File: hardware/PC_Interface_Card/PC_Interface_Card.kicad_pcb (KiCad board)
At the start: 2 copper layers, 85 parts, among them J1 GSB1C41110SSHR, J2 DM3BT-DSF-PEJS, J3 BM11B-GHS-TBT, SW1 CherryMX, SW2 CherryMX, SW3 CherryMX, SW4 CherryMX, SW5 CherryMX, SW6 TL1240YQ2JBLK, SW7 TL1240YQ2JBLK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

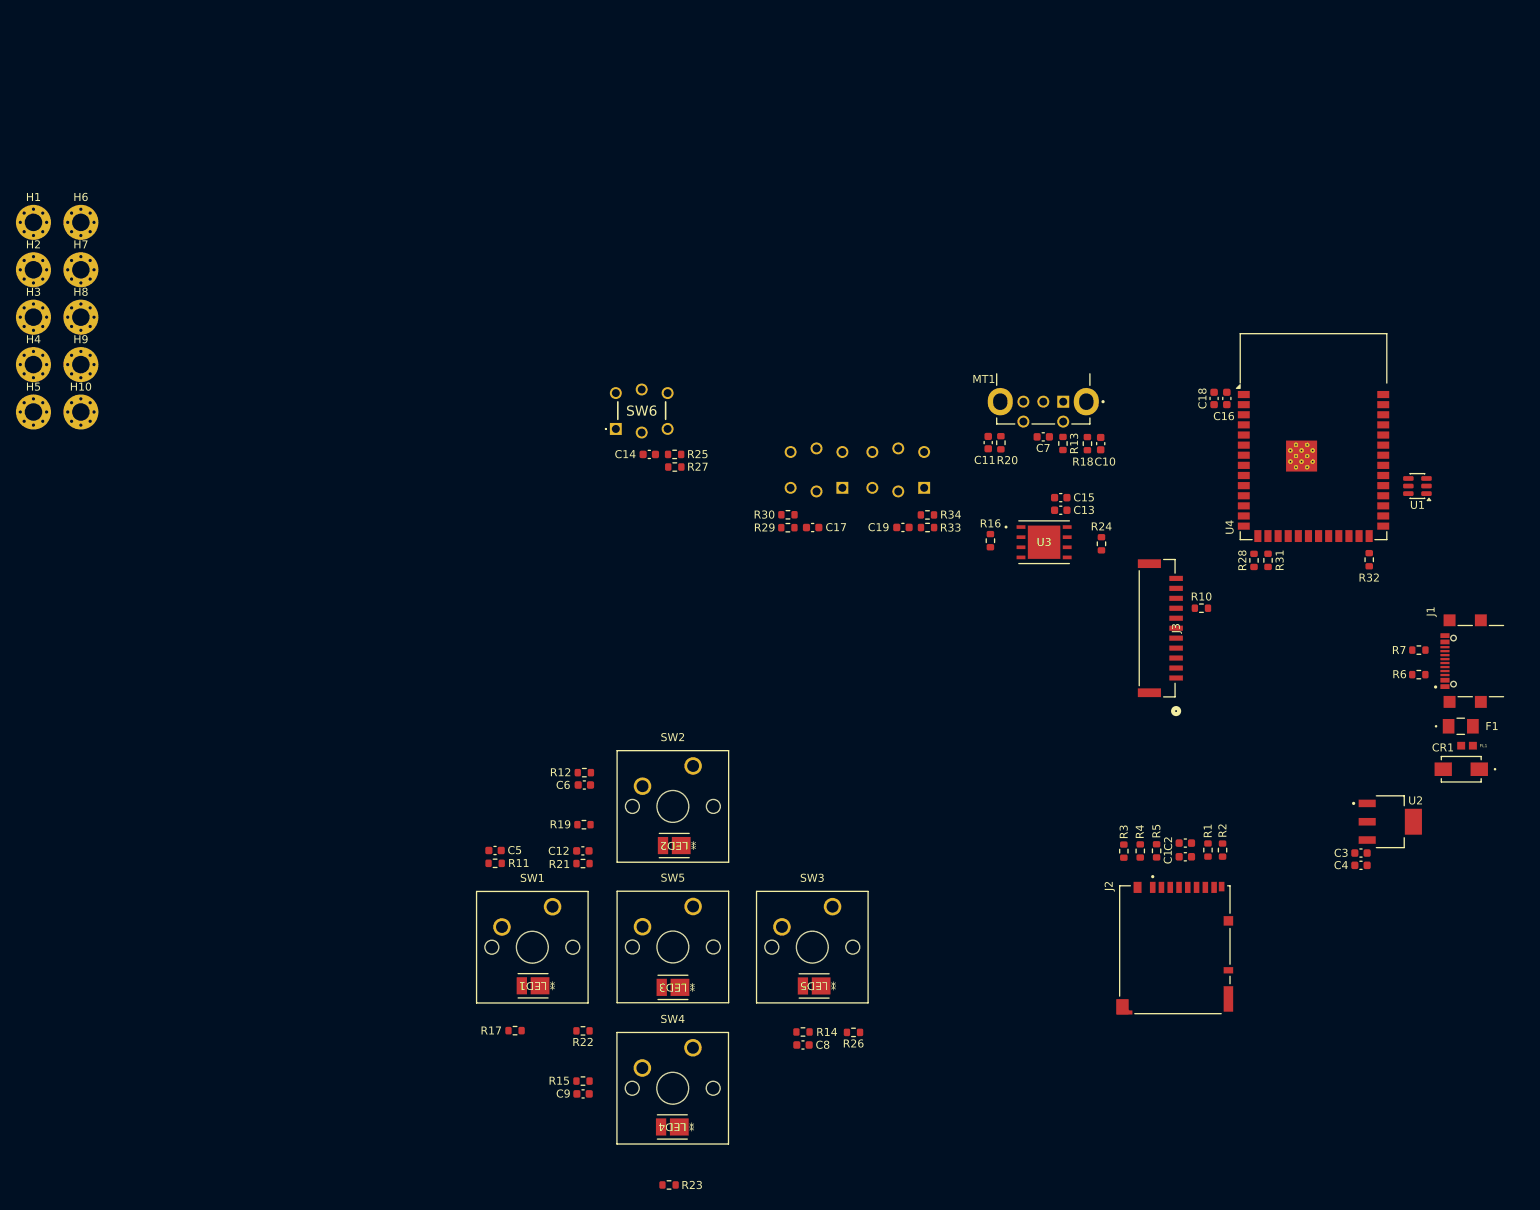
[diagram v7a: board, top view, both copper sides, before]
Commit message: Saving data for the day - added dxf for display and component placement
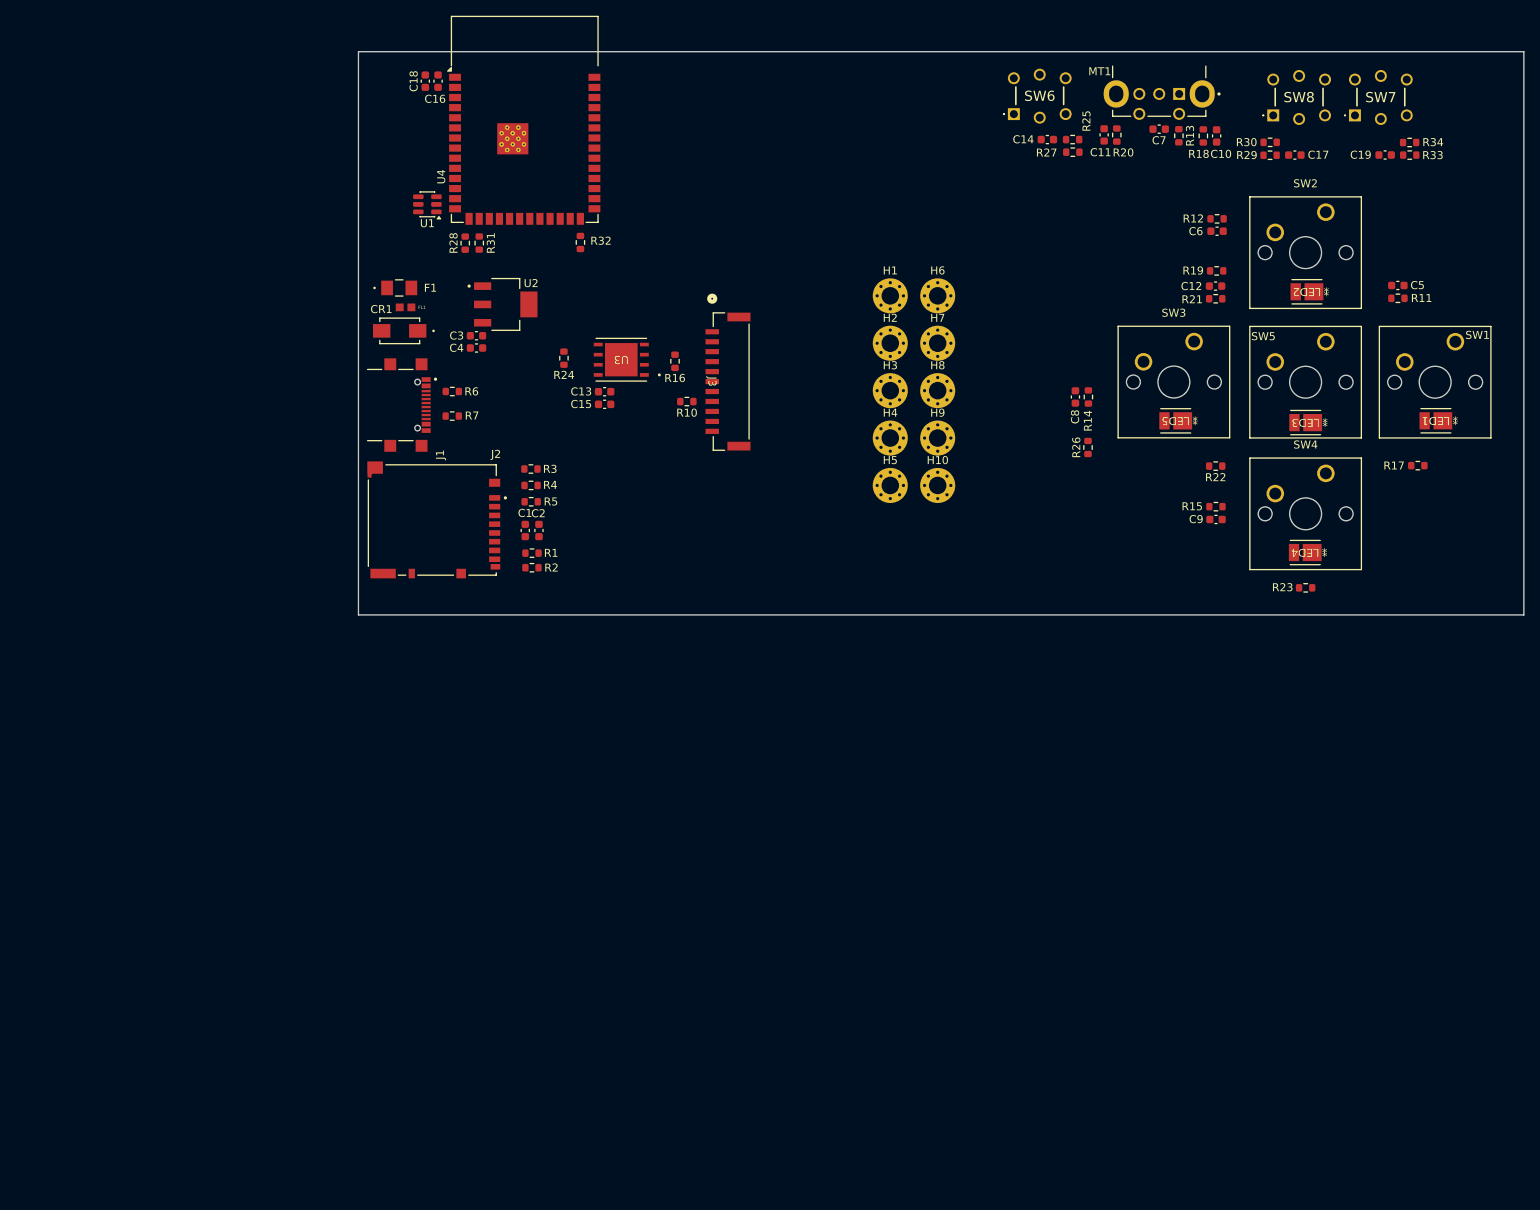
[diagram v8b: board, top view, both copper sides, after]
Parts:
- SW7, SW8: moved to F.Cu
- moved CR1 144.1 mm to (14.5, 33.3)
- moved F1 144.1 mm to (14.4, 27.9)
- moved FL1 144.1 mm to (15.2, 30.3)
- moved J1 139.0 mm to (14.1, 42.6), turned to -90 degrees
- moved C5 133.7 mm to (139.7, 27.6)
- moved LED1 133.7 mm to (144.5, 44.6)
- moved R11 133.7 mm to (139.7, 29.2)
- moved R17 133.7 mm to (142.2, 50.2)
- moved SW1 133.7 mm to (144.4, 39.7)
- moved U1 129.2 mm to (17.9, 17.4)
- moved C3 128.6 mm to (24.1, 33.9)
- moved C4 128.6 mm to (24.1, 35.4)
- moved U2 128.6 mm to (27.8, 30.0)
- moved R6 126.4 mm to (21.1, 40.9), turned to 0 degrees
- moved R7 124.8 mm to (21.1, 44.0), turned to 0 degrees
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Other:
- board outline added: 146.3 x 70.7 mm
- board text added: "Display Connector"
- board text added: "EN and BOOT Buttons"
- board text added: "Encoder"
- board text added: "FRAM"
- board text added: "LDO"
- board text added: "Play Pause"
- board text added: "SDMMC"
- board text added: "SW DOWN"
- board text added: "SW LEFT"
- board text added: "SW MENU"
- board text added: "SW RIGHT"
- board text added: "SW UP"
- board text added: "USB C"
- board text added: "USB Prot"
